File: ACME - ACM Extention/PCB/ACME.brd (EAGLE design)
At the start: 49 x 34 mm, 17 parts, among them IC1 Optocoupler DIP

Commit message: Small fixes
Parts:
- moved R4 5.23 mm to (28.7, 21.0)
- moved R3 2.52 mm to (16.1, 22.3)
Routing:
- net N$6: track 1.56 -> 7.26 mm
- net N$2: track 1.60 -> 3.17 mm
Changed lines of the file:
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@@
 <setting verticaltext="up"/>
 </settings>
-<grid distance="1" unitdist="mm" unit="mm" style="lines" multiple="1" display="yes" altdistance="0.01" altunitdist="mm" altunit="mm"/>
+<grid distance="0.5" unitdist="mm" unit="mm" style="lines" multiple="1" display="yes" altdistance="0.01" altunitdist="mm" altunit="mm"/>
 <layers>
 <layer number="1" name="Top" color="4" fill="1" visible="yes" active="yes"/>
@@
 <attribute name="RS_PRICE-STOCK" value="http://uk.rs-online.com/web/p/products/0186022P" x="22.4" y="20.85" size="1.778" layer="28" rot="MR270" display="off"/>
 </element>
-<element name="R3" library="ERA-3AEB2262V(0603 Resistor)" package="RESC1608X55N" value="200 Ohm" x="18.6" y="22.26" smashed="yes" rot="MR270">
-<attribute name="DESCRIPTION" value="Thin Film Resistors - SMD 0603 22.6Kohm 0.1% 25ppm" x="18.6" y="22.26" size="1.778" layer="28" rot="MR270" display="off"/>
-<attribute name="HEIGHT" value="0.55mm" x="18.6" y="22.26" size="1.778" layer="28" rot="MR270" display="off"/>
-<attribute name="MANUFACTURER_NAME" value="Panasonic" x="18.6" y="22.26" size="1.778" layer="28" rot="MR270" display="off"/>
-<attribute name="MANUFACTURER_PART_NUMBER" value="ERA-3AEB2262V" x="18.6" y="22.26" size="1.778" layer="28" rot="MR270" display="off"/>
-<attribute name="MOUSER_PART_NUMBER" value="667-ERA-3AEB2262V" x="18.6" y="22.26" size="1.778" layer="28" rot="MR270" display="off"/>
-<attribute name="MOUSER_PRICE-STOCK" value="https://www.mouser.com/Search/Refine.aspx?Keyword=667-ERA-3AEB2262V" x="18.6" y="22.26" size="1.778" layer="28" rot="MR270" display="off"/>
-<attribute name="NAME" x="20.39" y="22.41" size="1.27" layer="26" rot="MR180" align="center"/>
-<attribute name="RS_PART_NUMBER" value="" x="18.6" y="22.26" size="1.778" layer="28" rot="MR270" display="off"/>
-<attribute name="RS_PRICE-STOCK" value="" x="18.6" y="22.26" size="1.778" layer="28" rot="MR270" display="off"/>
-</element>
-<element name="R4" library="ERA-3AEB2262V(0603 Resistor)" package="RESC1608X55N" value="200 Ohm" x="23.66" y="22.3" smashed="yes" rot="SMR270">
-<attribute name="DESCRIPTION" value="Thin Film Resistors - SMD 0603 22.6Kohm 0.1% 25ppm" x="23.66" y="22.3" size="1.778" layer="28" rot="SMR270" display="off"/>
-<attribute name="HEIGHT" value="0.55mm" x="23.66" y="22.3" size="1.778" layer="28" rot="SMR270" display="off"/>
-<attribute name="MANUFACTURER_NAME" value="Panasonic" x="23.66" y="22.3" size="1.778" layer="28" rot="SMR270" display="off"/>
-<attribute name="MANUFACTURER_PART_NUMBER" value="ERA-3AEB2262V" x="23.66" y="22.3" size="1.778" layer="28" rot="SMR270" display="off"/>
-<attribute name="MOUSER_PART_NUMBER" value="667-ERA-3AEB2262V" x="23.66" y="22.3" size="1.778" layer="28" rot="SMR270" display="off"/>
-<attribute name="MOUSER_PRICE-STOCK" value="https://www.mouser.com/Search/Refine.aspx?Keyword=667-ERA-3AEB2262V" x="23.66" y="22.3" size="1.778" layer="28" rot="SMR270" display="off"/>
-<attribute name="NAME" x="25.47" y="22.44" size="1.27" layer="26" rot="SMR0" align="center"/>
-<attribute name="RS_PART_NUMBER" value="" x="23.66" y="22.3" size="1.778" layer="28" rot="SMR270" display="off"/>
-<attribute name="RS_PRICE-STOCK" value="" x="23.66" y="22.3" size="1.778" layer="28" rot="SMR270" display="off"/>
+<element name="R3" library="ERA-3AEB2262V(0603 Resistor)" package="RESC1608X55N" value="200 Ohm" x="16.08" y="22.26" smashed="yes" rot="MR270">
+<attribute name="DESCRIPTION" value="Thin Film Resistors - SMD 0603 22.6Kohm 0.1% 25ppm" x="16.08" y="22.26" size="1.778" layer="28" rot="MR270" display="off"/>
+<attribute name="HEIGHT" value="0.55mm" x="16.08" y="22.26" size="1.778" layer="28" rot="MR270" display="off"/>
+<attribute name="MANUFACTURER_NAME" value="Panasonic" x="16.08" y="22.26" size="1.778" layer="28" rot="MR270" display="off"/>
+<attribute name="MANUFACTURER_PART_NUMBER" value="ERA-3AEB2262V" x="16.08" y="22.26" size="1.778" layer="28" rot="MR270" display="off"/>
+<attribute name="MOUSER_PART_NUMBER" value="667-ERA-3AEB2262V" x="16.08" y="22.26" size="1.778" layer="28" rot="MR270" display="off"/>
+<attribute name="MOUSER_PRICE-STOCK" value="https://www.mouser.com/Search/Refine.aspx?Keyword=667-ERA-3AEB2262V" x="16.08" y="22.26" size="1.778" layer="28" rot="MR270" display="off"/>
+<attribute name="NAME" x="14.07" y="22.66" size="1.27" layer="26" rot="MR180" align="center"/>
+<attribute name="RS_PART_NUMBER" value="" x="16.08" y="22.26" size="1.778" layer="28" rot="MR270" display="off"/>
+<attribute name="RS_PRICE-STOCK" value="" x="16.08" y="22.26" size="1.778" layer="28" rot="MR270" display="off"/>
+</element>
+<element name="R4" library="ERA-3AEB2262V(0603 Resistor)" package="RESC1608X55N" value="200 Ohm" x="28.72" y="20.96" smashed="yes" rot="SMR270">
+<attribute name="DESCRIPTION" value="Thin Film Resistors - SMD 0603 22.6Kohm 0.1% 25ppm" x="28.72" y="20.96" size="1.778" layer="28" rot="SMR270" display="off"/>
+<attribute name="HEIGHT" value="0.55mm" x="28.72" y="20.96" size="1.778" layer="28" rot="SMR270" display="off"/>
+<attribute name="MANUFACTURER_NAME" value="Panasonic" x="28.72" y="20.96" size="1.778" layer="28" rot="SMR270" display="off"/>
+<attribute name="MANUFACTURER_PART_NUMBER" value="ERA-3AEB2262V" x="28.72" y="20.96" size="1.778" layer="28" rot="SMR270" display="off"/>
+<attribute name="MOUSER_PART_NUMBER" value="667-ERA-3AEB2262V" x="28.72" y="20.96" size="1.778" layer="28" rot="SMR270" display="off"/>
+<attribute name="MOUSER_PRICE-STOCK" value="https://www.mouser.com/Search/Refine.aspx?Keyword=667-ERA-3AEB2262V" x="28.72" y="20.96" size="1.778" layer="28" rot="SMR270" display="off"/>
+<attribute name="NAME" x="30.53" y="21.1" size="1.27" layer="26" rot="SMR0" align="center"/>
+<attribute name="RS_PART_NUMBER" value="" x="28.72" y="20.96" size="1.778" layer="28" rot="SMR270" display="off"/>
+<attribute name="RS_PRICE-STOCK" value="" x="28.72" y="20.96" size="1.778" layer="28" rot="SMR270" display="off"/>
 </element>
 <element name="R5" library="ERA-3AEB2262V(0603 Resistor)" package="RESC1608X55N" value="1K Ohm" x="16.96" y="15.09" smashed="yes" rot="MR0">
@@
 <contactref element="IC1" pad="1"/>
 <contactref element="R3" pad="1"/>
-<wire x1="18.6" y1="23.06" x2="18.6" y2="24.65" width="1" layer="16"/>
-<wire x1="18.6" y1="24.65" x2="18.59" y2="24.66" width="1" layer="16"/>
+<wire x1="18.59" y1="24.66" x2="16.99" y2="23.06" width="1" layer="16"/>
+<wire x1="16.99" y1="23.06" x2="16.08" y2="23.06" width="1" layer="16"/>
 </signal>
 <signal name="N$6">
 <contactref element="IC1" pad="3"/>
 <contactref element="R4" pad="1"/>
-<wire x1="23.66" y1="23.1" x2="23.66" y2="24.65" width="1" layer="16"/>
-<wire x1="23.66" y1="24.65" x2="23.67" y2="24.66" width="1" layer="16"/>
+<wire x1="28.72" y1="21.76" x2="24.84" y2="21.76" width="1" layer="16"/>
+<wire x1="24.84" y1="21.76" x2="23.67" y2="22.93" width="1" layer="16"/>
+<wire x1="23.67" y1="24.66" x2="23.67" y2="22.93" width="1" layer="16"/>
 </signal>
 <signal name="N$7">
@@
 <wire x1="45.4268" y1="17.1068" x2="43.64" y2="15.32" width="0.5" layer="16"/>
 <wire x1="45.4268" y1="22.01409375" x2="44.40409375" y2="23.0368" width="0.5" layer="16"/>
-<wire x1="18.6" y1="21.46" x2="14.49219375" y2="21.46" width="0.85" layer="16"/>
+<wire x1="16.08" y1="21.46" x2="14.49219375" y2="21.46" width="0.85" layer="16"/>
 <wire x1="6.69219375" y1="13.66" x2="6.69" y2="13.66" width="0.85" layer="16"/>
 <wire x1="14.49219375" y1="21.46" x2="6.69219375" y2="13.66" width="0.85" layer="16"/>
-<wire x1="18.6" y1="21.46" x2="18.6211" y2="21.4811" width="0.85" layer="16"/>
+<wire x1="16.08" y1="21.46" x2="16.1011" y2="21.4811" width="0.85" layer="16"/>
 <wire x1="22.3921" y1="25.3137625" x2="23.0862375" y2="26.0079" width="0.85" layer="16"/>
 <wire x1="23.0862375" y1="26.0079" x2="24.1737625" y2="26.0079" width="0.85" layer="16"/>
@@
 <wire x1="24.9579" y1="25.2237625" x2="24.9579" y2="24.18714375" width="0.85" layer="16"/>
 <wire x1="24.9579" y1="24.18714375" x2="25.97324375" y2="23.1718" width="0.85" layer="16"/>
-<wire x1="18.6211" y1="21.4811" x2="20.0949625" y2="21.4811" width="0.85" layer="16"/>
+<wire x1="16.1011" y1="21.4811" x2="20.0949625" y2="21.4811" width="0.85" layer="16"/>
 <wire x1="20.0949625" y1="21.4811" x2="22.3921" y2="23.7782375" width="0.85" layer="16"/>
 <wire x1="44.40409375" y1="23.0368" x2="36.135" y2="23.0368" width="0.5" layer="16"/>
@@
 <wire x1="44.7579" y1="19.0648125" x2="43.64" y2="17.9469125" width="0.5" layer="16"/>
 <wire x1="44.0551875" y1="22.4279" x2="36.2696625" y2="22.4279" width="0.5" layer="16"/>
-<wire x1="8.17" y1="13.73" x2="14.0911" y2="19.6511" width="0.85" layer="16"/>
+<wire x1="8.17" y1="13.73" x2="14.5611" y2="20.1211" width="0.85" layer="16"/>
 <wire x1="8.17" y1="12" x2="7.29" y2="11.12" width="0.85" layer="16"/>
 <wire x1="6.69" y1="11.12" x2="7.29" y2="11.12" width="0.85" layer="16"/>
 <wire x1="8.17" y1="12" x2="8.17" y2="13.73" width="0.85" layer="16"/>
-<wire x1="14.0911" y1="19.6511" x2="21.8111" y2="19.6511" width="0.85" layer="16"/>
-<wire x1="21.8111" y1="19.6511" x2="23.66" y2="21.5" width="0.85" layer="16"/>
-<wire x1="35.4017625" y1="21.56" x2="23.72" y2="21.56" width="0.85" layer="16"/>
-<wire x1="23.72" y1="21.56" x2="23.66" y2="21.5" width="0.85" layer="16"/>
+<wire x1="14.5611" y1="20.1211" x2="28.6811" y2="20.1211" width="0.85" layer="16"/>
+<wire x1="28.6811" y1="20.1211" x2="28.72" y2="20.16" width="0.85" layer="16"/>
+<wire x1="35.4017625" y1="21.56" x2="31.18" y2="21.56" width="0.85" layer="16"/>
+<wire x1="31.18" y1="21.56" x2="29.78" y2="20.16" width="0.85" layer="16"/>
+<wire x1="29.78" y1="20.16" x2="28.72" y2="20.16" width="0.85" layer="16"/>
 <wire x1="36.2696625" y1="22.4279" x2="35.4017625" y2="21.56" width="0.5" layer="16"/>
 </signal>

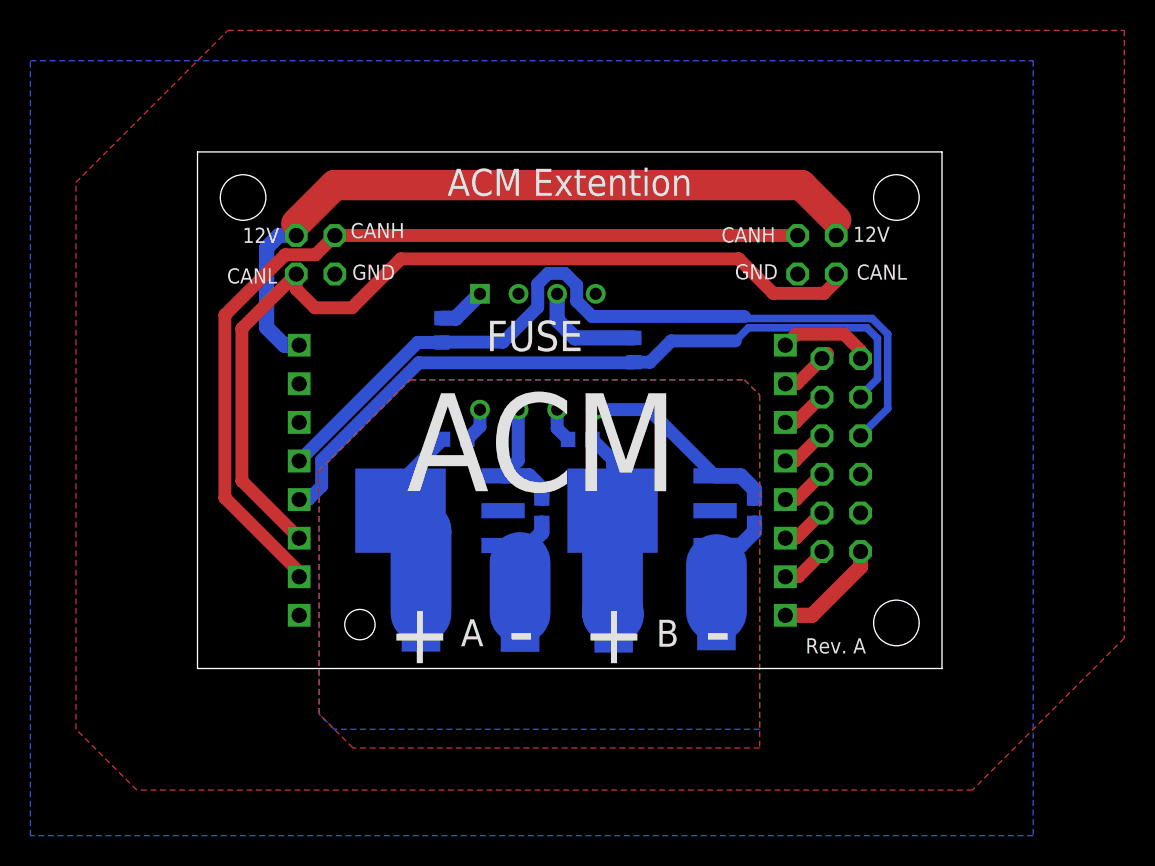
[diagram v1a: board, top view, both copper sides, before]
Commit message: ACME: Changed PWM Routing for isolation
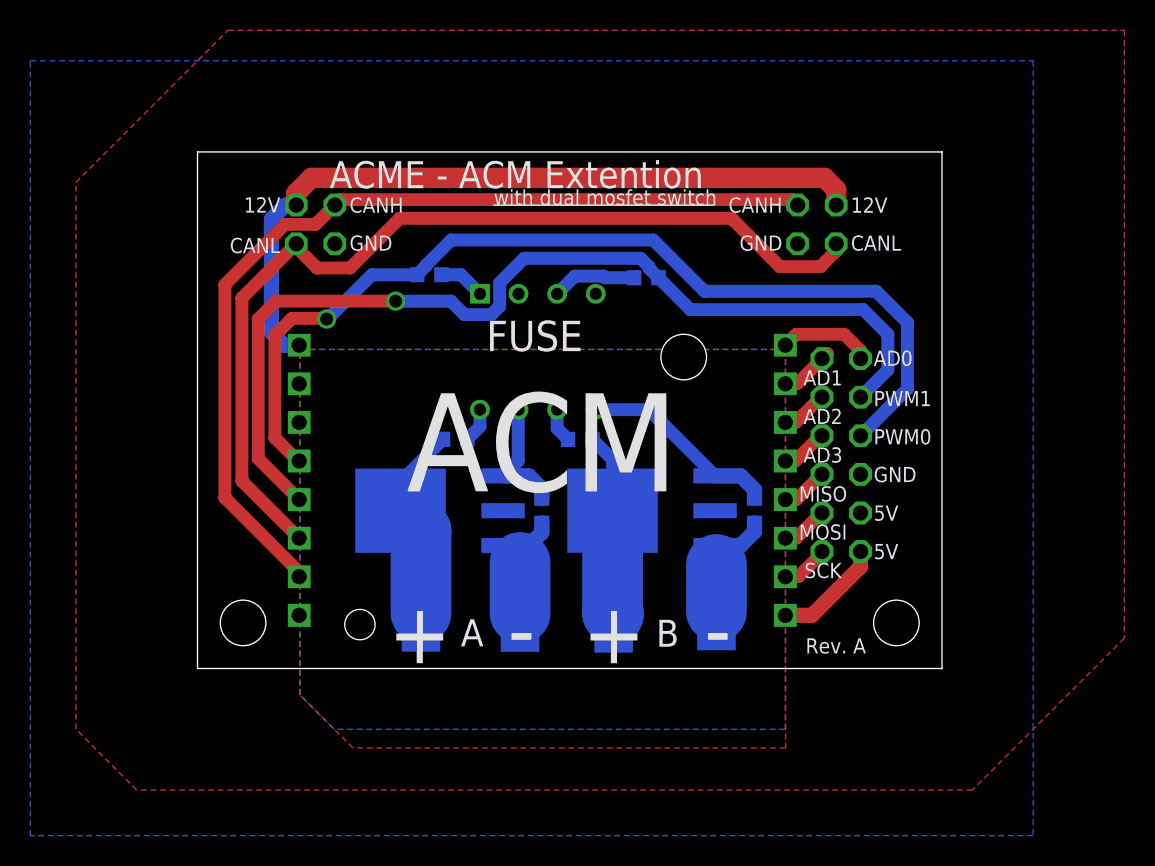
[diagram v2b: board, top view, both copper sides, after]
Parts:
- moved R4 4.83 mm to (29.5, 25.7), turned to 180 degrees
- moved R3 3.75 mm to (15.3, 25.9), turned to 0 degrees
- moved U$3 2.00 mm to (6.50, 30.5)
- moved U$4 2.00 mm to (39.5, 30.5)
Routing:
- net PWM1: track 48.4 -> 64.7 mm, vias 0 -> 1
- net PWM0: track 54.4 -> 64.2 mm, vias 0 -> 1
- net CANH: track 59.1 -> 61.4 mm
- net CANL: track 60.5 -> 62.3 mm
- net N$6: track 7.26 -> 5.60 mm
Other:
- board text added: "*Designed by Humans from Earth*"
- board text added: "5V"
- board text added: "ACME - ACM Extention"
- board text added: "AD0"
- board text added: "AD1"
- board text added: "AD2"
- board text added: "AD3"
- board text added: "MISO"
- board text added: "MOSI"
- board text added: "PWM0"
- board text added: "PWM1"
- board text added: "SCK"
- board text added: "v3.2"
- board text added: "with dual mosfet switch"
- board text removed: "ACM Extention"

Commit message: ACME: Silkcreeen and copper pour settings for isolation
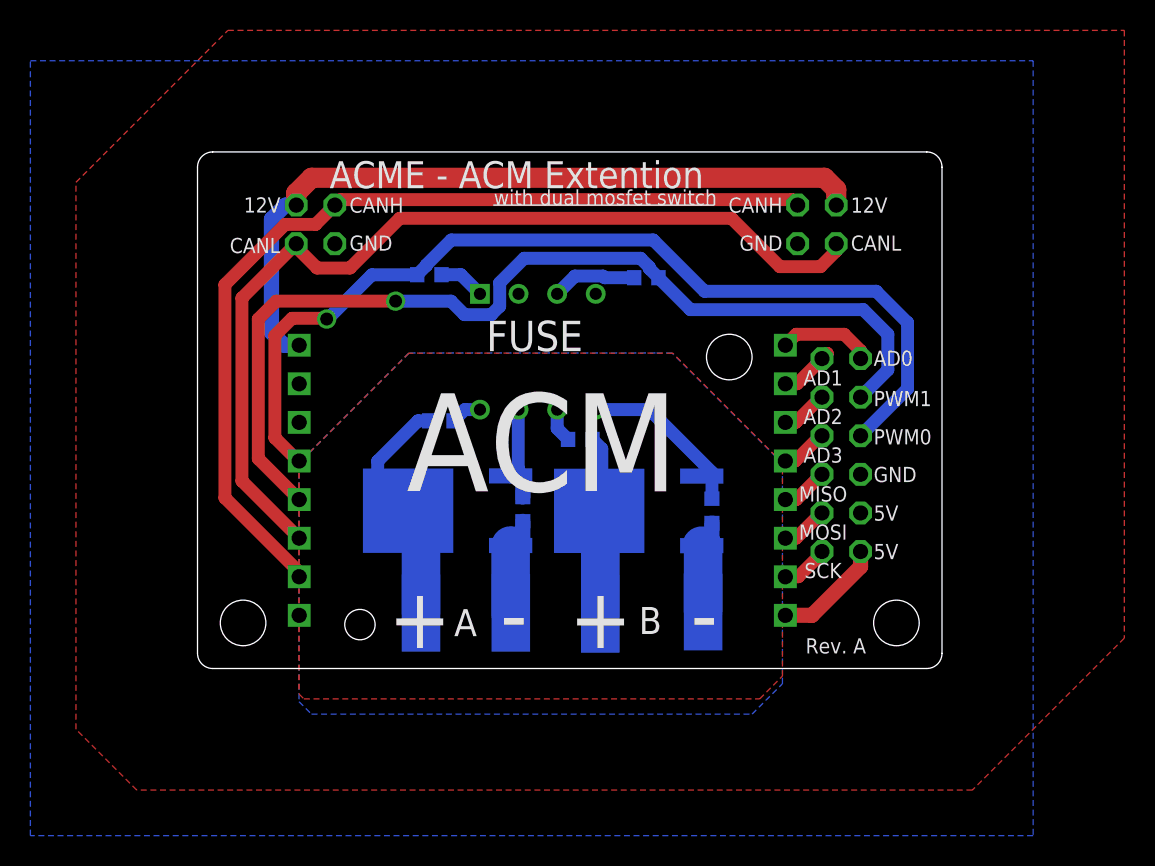
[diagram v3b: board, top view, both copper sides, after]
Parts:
- Q1, Q2: value (none) -> NGD8201ANT4G
- moved R1 2.80 mm to (33.9, 10.4)
- moved R5 1.51 mm to (16.1, 16.3)
- moved R2 1.25 mm to (21.4, 10.5)
- moved Q2 0.88 mm to (29.0, 10.4)
- moved D1 0.88 mm to (26.5, 3.58)
- moved S1 0.88 mm to (33.3, 3.73)
- moved S0 0.61 mm to (20.6, 3.65)
- moved Q1 0.50 mm to (16.5, 10.4)
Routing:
- net DRAIN0: track 13.2 -> 15.7 mm
- net GATE1: track 13.2 -> 11.1 mm
- net GATE0: track 8.33 -> 6.77 mm
- net SOURCE0: track 8.47 -> 6.92 mm
- net SOURCE1: track 7.94 -> 6.56 mm
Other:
- outline, holes or cut-outs redrawn

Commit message: ACME: Fixed DRC
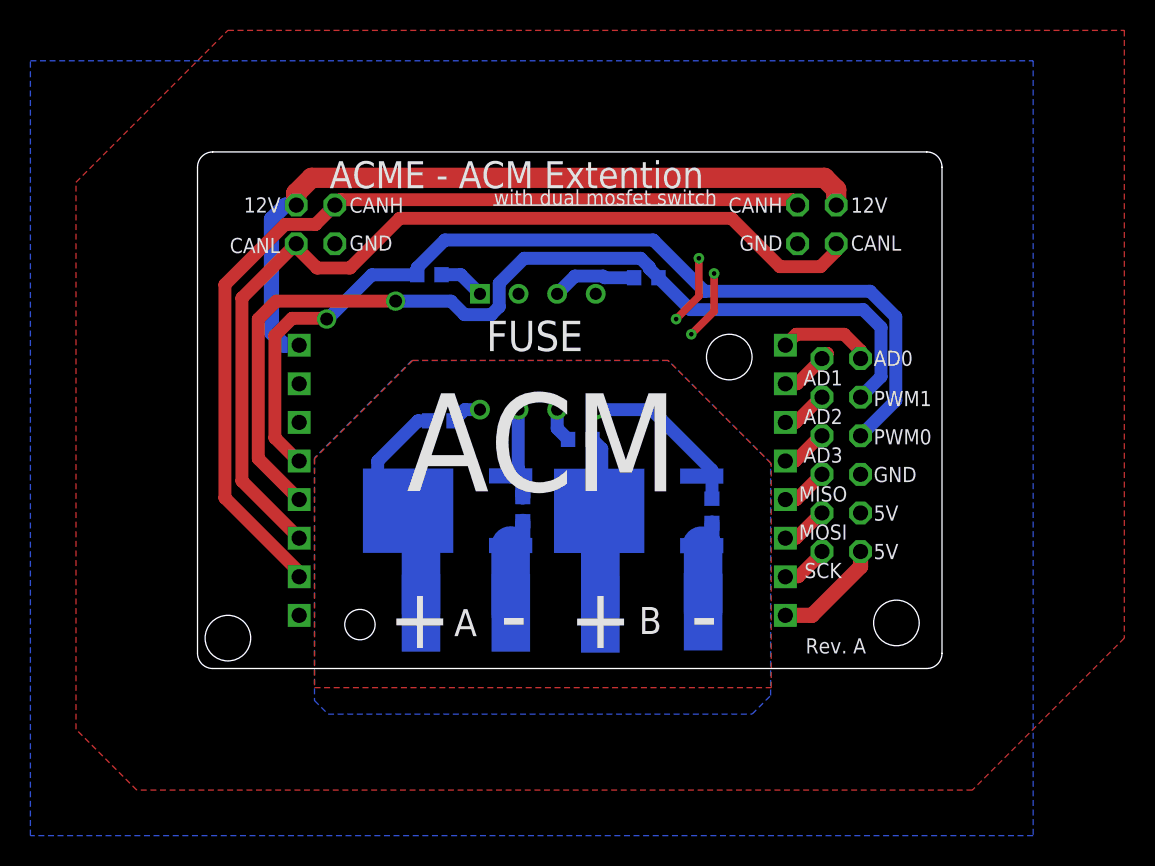
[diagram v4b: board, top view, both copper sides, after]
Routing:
- net GND: track 0.00 -> 9.24 mm, vias 0 -> 4
- net PWM0: track 64.2 -> 63.6 mm
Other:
- board text added: "v3.8"
- board text removed: "v3.2"
